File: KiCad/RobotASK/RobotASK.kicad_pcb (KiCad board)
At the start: 2 copper layers, 80 x 50 mm, 13 parts, among them J1 Conn_01x04_Pin, J2 Conn_01x04_Pin, J3 Conn_01x04_Pin, J4 Conn_01x04_Pin, J5 Conn_01x04_Pin, J6 Conn_01x04_Pin, J7 Conn_01x02_Pin, SW2 SW_Omron_B3FS, U1 ATmega328-P, Y1 16MHz

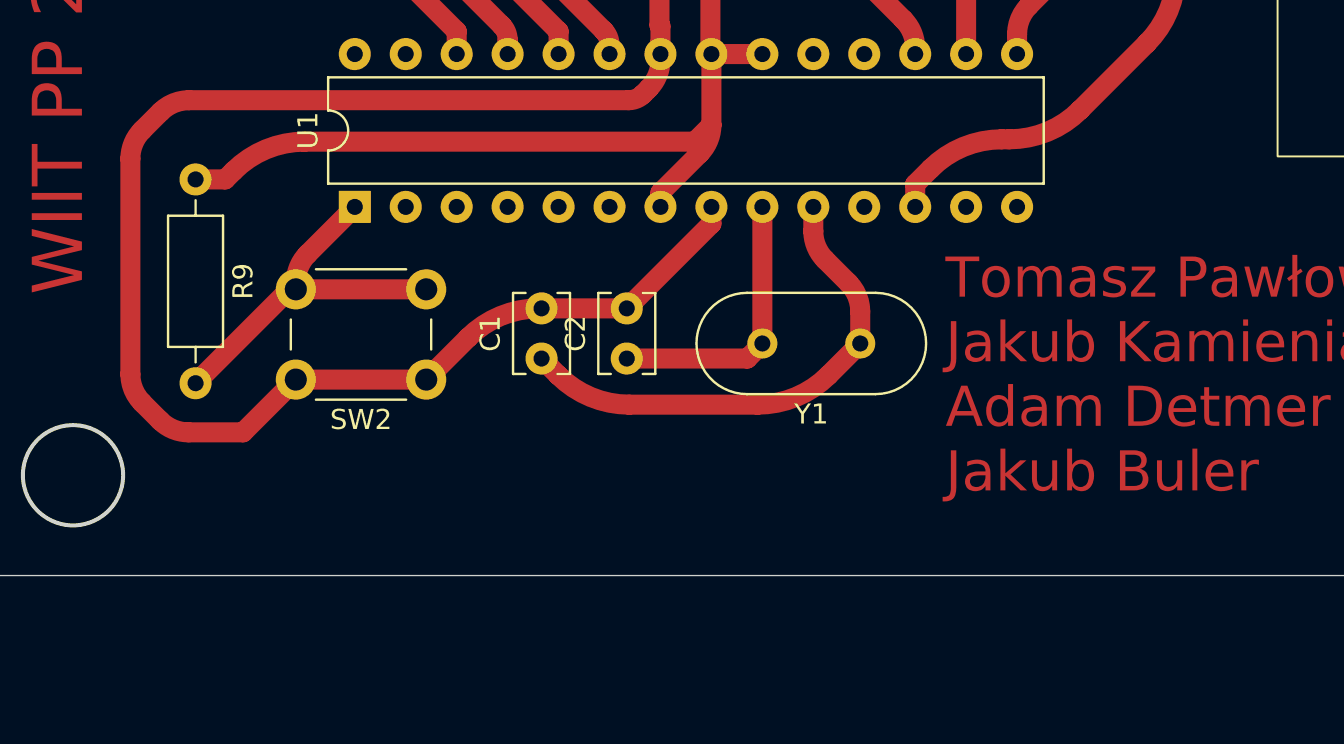
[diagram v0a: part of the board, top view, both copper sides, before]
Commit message: Add pins to quickly reprogram the microprocessor
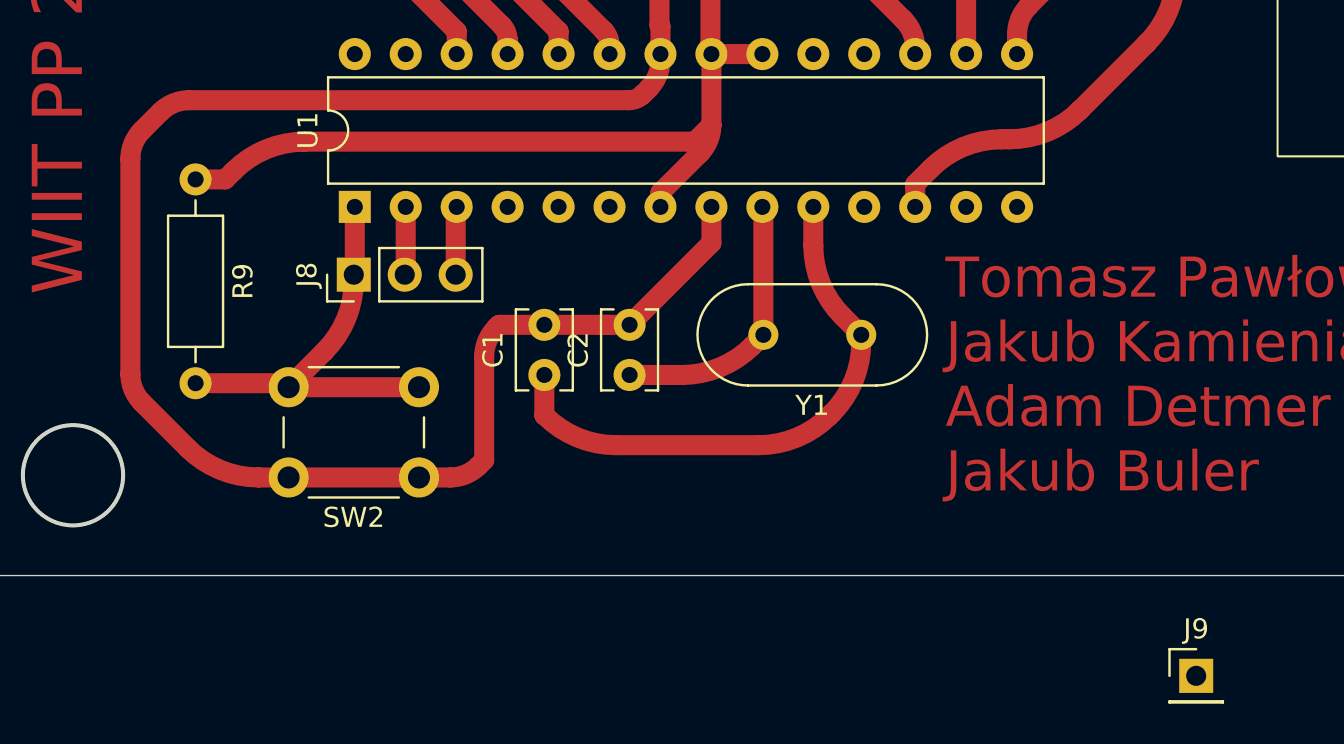
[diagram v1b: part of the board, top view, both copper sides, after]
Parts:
- added J8: Conn_01x03_Pin, Connector_PinHeader_2.54mm:PinHeader_1x03_P2.54mm_Vertical, F.Cu at (89.0, 85.0)
- added J9: Conn_01x01_Pin, Connector_PinHeader_2.54mm:PinHeader_1x01_P2.54mm_Vertical, F.Cu at (131.0, 105.0)
- moved SW2 4.89 mm to (92.2, 95.1)
- moved C1 0.83 mm to (98.5, 90.0)
- moved C2 0.83 mm to (102.8, 90.0)
- moved Y1 0.43 mm to (114.3, 88.0)
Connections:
- U1 pad 2: unconnected-(U1-PD0-Pad2) -> RX
- U1 pad 3: unconnected-(U1-PD1-Pad3) -> TX
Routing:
- net GND: track 156.4 -> 162.7 mm
- net TX: track 0.00 -> 3.40 mm
- net RX: track 0.00 -> 3.40 mm
- net CRY2: track 25.2 -> 28.5 mm
- net ~RESET: track 19.0 -> 21.3 mm

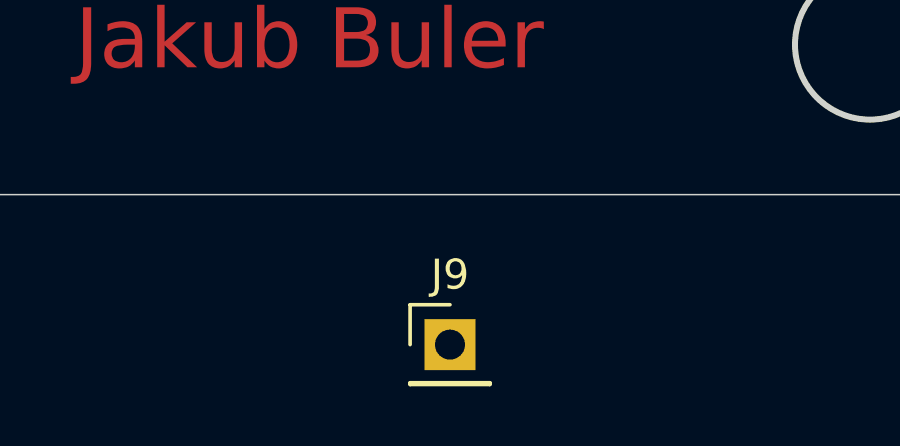
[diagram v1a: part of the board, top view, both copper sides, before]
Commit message: Bez zbędnego pinu GND, update KiCad 8, export ze ścieżkami
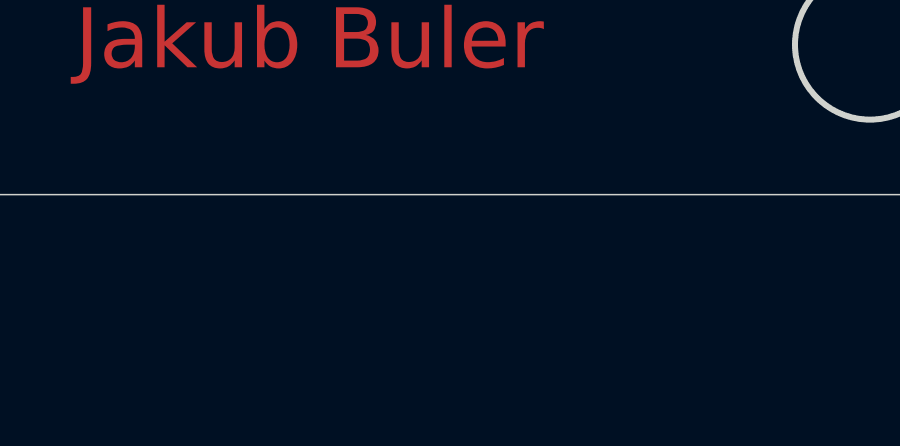
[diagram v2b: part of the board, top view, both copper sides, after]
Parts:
- removed J9: Conn_01x01_Pin, Connector_PinHeader_2.54mm:PinHeader_1x01_P2.54mm_Vertical

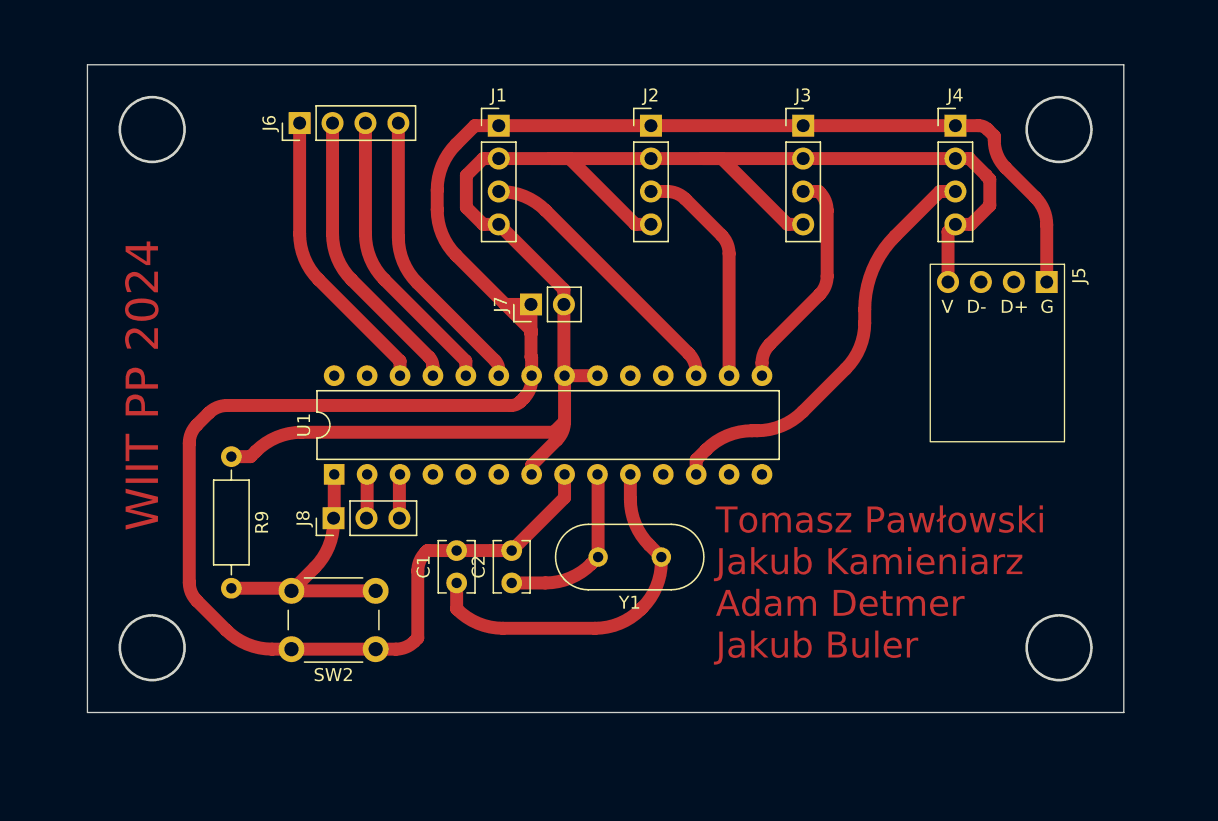
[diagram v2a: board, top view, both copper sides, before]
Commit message: Edit pcb layers
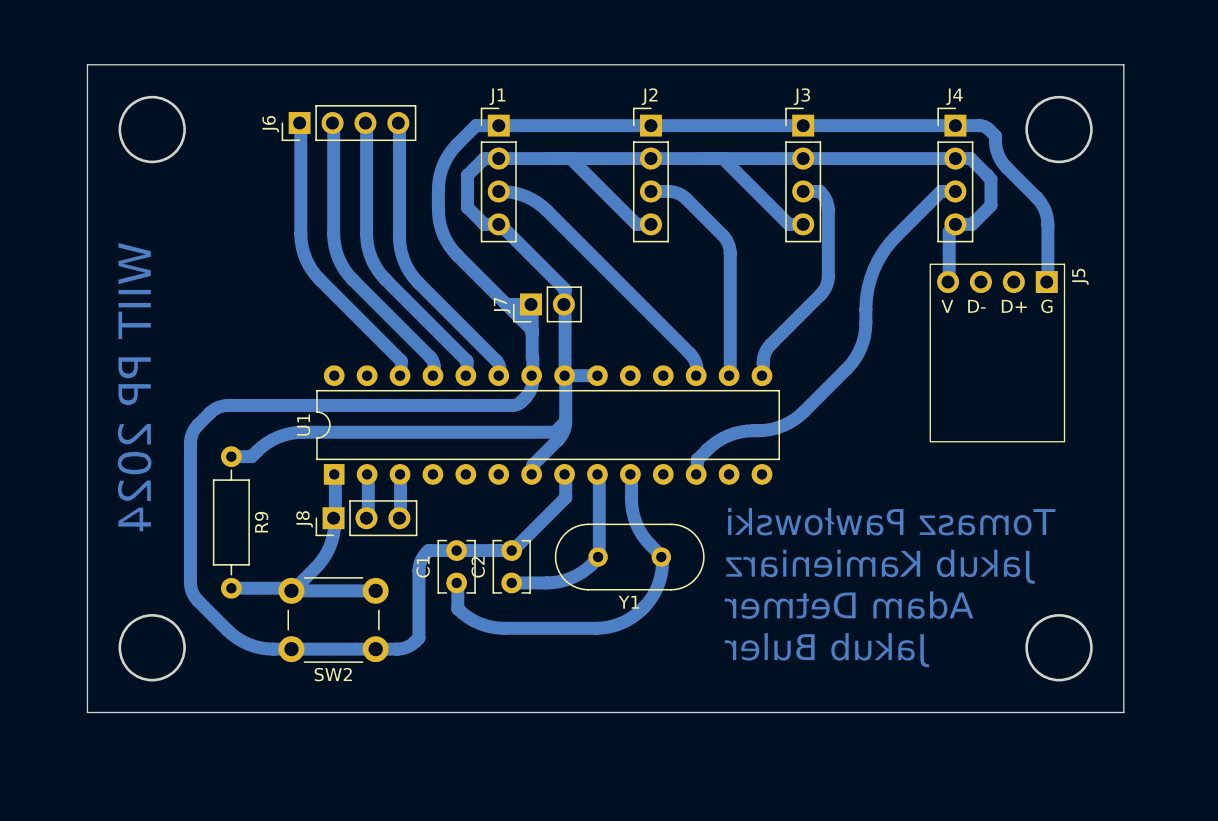
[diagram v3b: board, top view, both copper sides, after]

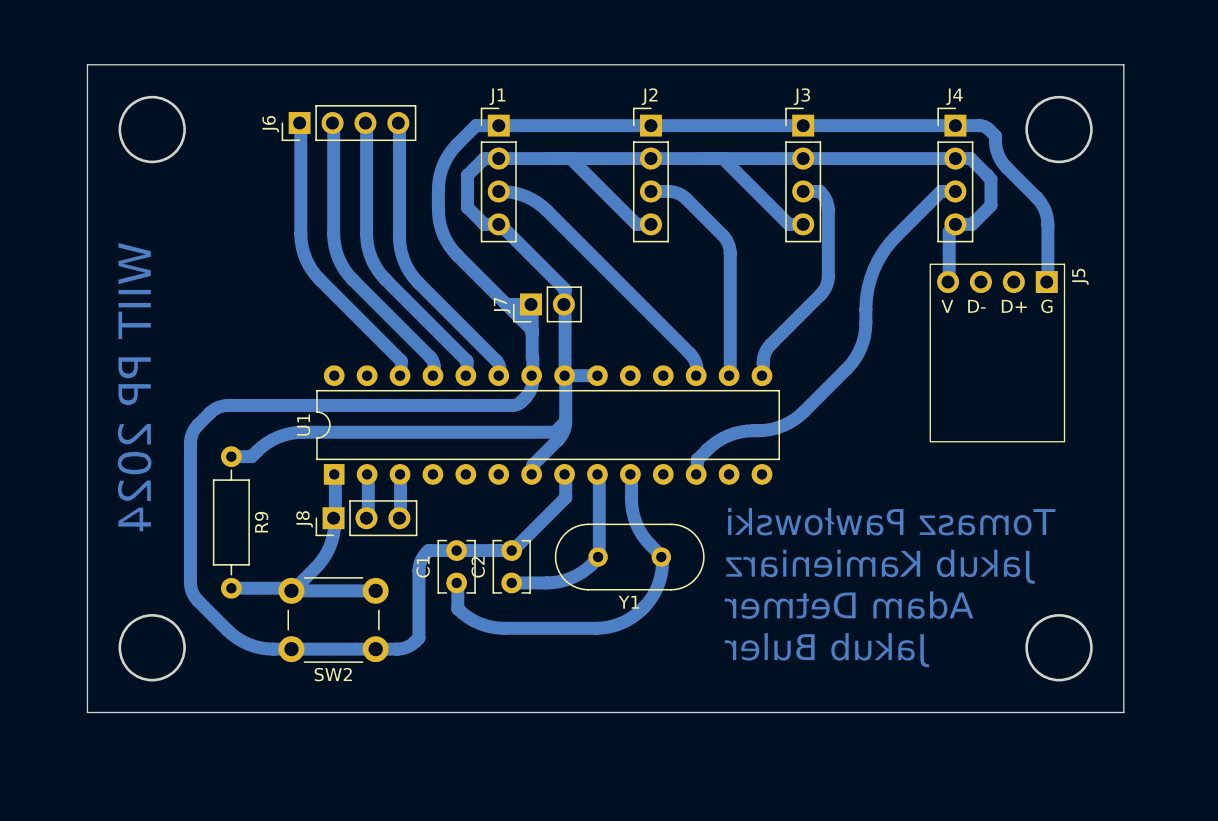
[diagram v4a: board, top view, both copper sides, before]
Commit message: Widen all possible traces, fill edge cuts layer, widen photoresistor PCB by 2mm
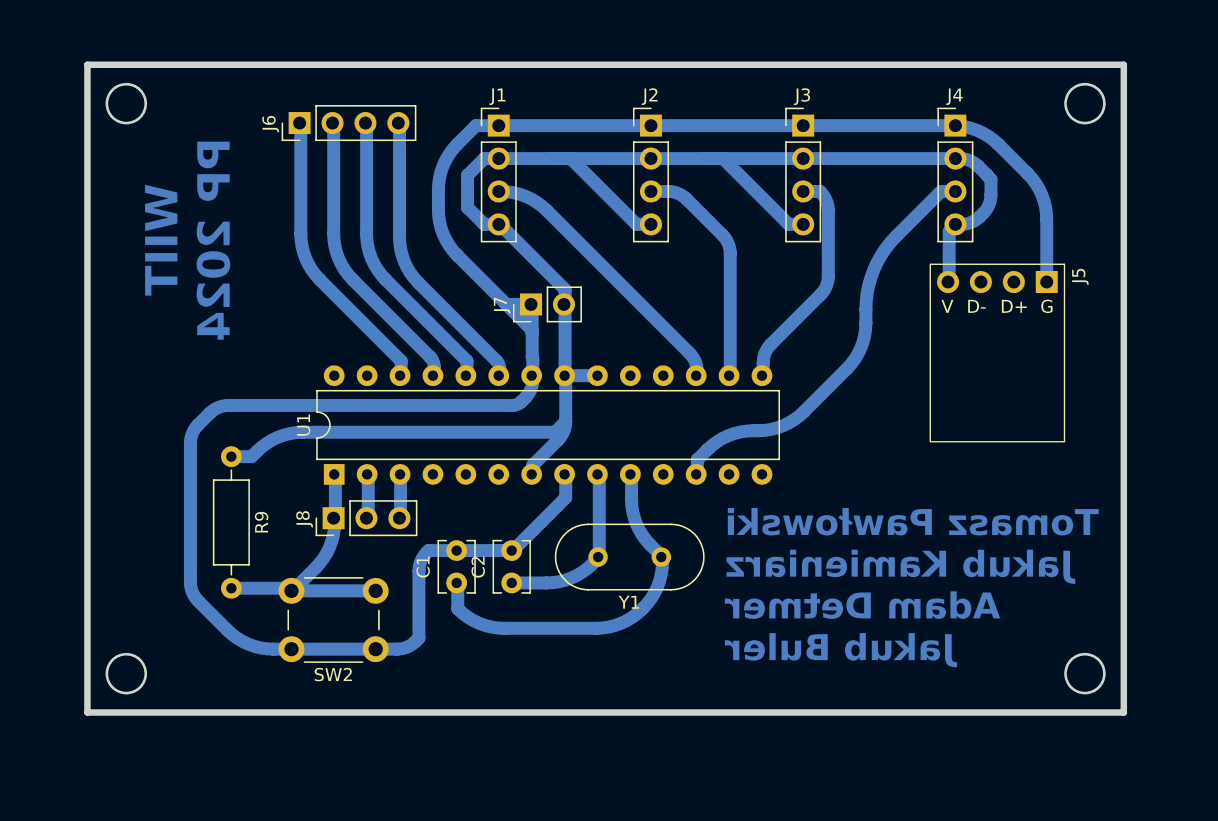
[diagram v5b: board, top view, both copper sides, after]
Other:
- outline, holes or cut-outs redrawn
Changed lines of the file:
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@@
 			(dxfimperialunits yes)
 			(dxfusepcbnewfont yes)
-			(psnegative no)
+			(psnegative yes)
 			(psa4output no)
 			(plotreference yes)
@@
 			(drillshape 1)
 			(scaleselection 1)
-			(outputdirectory "../../wydruki/Termotransfer/")
+			(outputdirectory "../../wydruki/UV/")
 		)
 	)
@@
 	)
 	(gr_circle
-		(center 75 95)
-		(end 77.5 95)
+		(center 73 97)
+		(end 74.5 97)
 		(locked yes)
 		(stroke
@@
 			(type solid)
 		)
-		(fill none)
+		(fill solid)
 		(layer "Edge.Cuts")
 	)
@@
 		(locked yes)
 		(stroke
-			(width 0.05)
+			(width 0.5)
 			(type default)
 		)
@@
 	)
 	(gr_circle
-		(center 145 95)
-		(end 147.5 95)
+		(center 147 97)
+		(end 148.5 97)
 		(locked yes)
 		(stroke
@@
 			(type solid)
 		)
-		(fill none)
+		(fill solid)
 		(layer "Edge.Cuts")
 	)
 	(gr_circle
-		(center 145 55)
-		(end 147.5 55)
+		(center 147 53)
+		(end 148.5 53)
 		(locked yes)
 		(stroke
@@
 			(type solid)
 		)
-		(fill none)
+		(fill solid)
 		(layer "Edge.Cuts")
 	)
 	(gr_circle
-		(center 75 55)
-		(end 77.5 55)
+		(center 73 53)
+		(end 74.5 53)
 		(locked yes)
 		(stroke
@@
 			(type solid)
 		)
-		(fill none)
+		(fill solid)
 		(layer "Edge.Cuts")
 	)
@@
 			(font
 				(size 2 2)
-				(thickness 0.15)
+				(thickness 0.5)
+				(bold yes)
 			)
 			(justify right bottom mirror)
 		)
 	)
-	(gr_text "WIIT PP 2024"
-		(at 75.2 86.2 90)
+	(gr_text "WIIT\nPP 2024"
+		(at 81.28 63.5 90)
 		(layer "B.Cu")
 		(effects
 			(font
 				(size 2.5 2.5)
-				(thickness 0.15)
+				(thickness 0.625)
+				(bold yes)
 			)
-			(justify right bottom mirror)
+			(justify bottom mirror)
 		)
 	)
@@
 	)
 	(segment
+		(start 99.99 54.7)
+		(end 136.804718 54.7)
+		(width 1)
+		(layer "B.Cu")
+		(net 2)
+	)
+	(segment
 		(start 104.33 70.75)
 		(end 104.33 72.561068)
@@
 	)
 	(segment
-		(start 139.582893 54.992893)
-		(end 140.09 55.5)
-		(width 1)
-		(layer "B.Cu")
-		(net 2)
-	)
-	(segment
 		(start 96.175787 87.664213)
 		(end 96.34 87.5)
@@
 	)
 	(segment
-		(start 137.09 54.7)
-		(end 101.84 54.7)
-		(width 1)
-		(layer "B.Cu")
-		(net 2)
-	)
-	(segment
 		(start 104.33 68.5)
 		(end 102.34 68.5)
@@
 	)
 	(segment
-		(start 101.84 54.7)
-		(end 99.99 54.7)
-		(width 1)
-		(layer "B.Cu")
-		(net 2)
-	)
-	(segment
 		(start 101.34 87.5)
 		(end 98.59 87.5)
@@
 	)
 	(segment
-		(start 99.99 54.7)
-		(end 98.554466 56.135534)
-		(width 1)
-		(layer "B.Cu")
-		(net 2)
-	)
-	(segment
 		(start 102.84 87.5)
 		(end 106.92 83.42)
@@
 	)
 	(segment
-		(start 144.14 62.363709)
-		(end 144.14 66.77)
-		(width 1)
-		(layer "B.Cu")
-		(net 2)
-	)
-	(segment
-		(start 140.96868 57.949748)
-		(end 143.261321 60.242389)
-		(width 1)
-		(layer "B.Cu")
-		(net 2)
-	)
-	(segment
-		(start 102.34 68.5)
-		(end 98.554466 64.714466)
-		(width 1)
-		(layer "B.Cu")
-		(net 2)
-	)
-	(segment
 		(start 92.34 95.11)
 		(end 85.84 95.11)
@@
 	)
 	(segment
-		(start 140.09 55.5)
-		(end 140.09 55.828427)
-		(width 1)
-		(layer "B.Cu")
-		(net 2)
-	)
-	(segment
 		(start 95.59 94.25)
 		(end 95.59 89.078427)
@@
 	)
 	(segment
-		(start 137.09 54.7)
-		(end 138.875786 54.7)
+		(start 97.09 61.178932)
+		(end 97.09 59.671068)
 		(width 1)
 		(layer "B.Cu")
@@
 	)
 	(segment
-		(start 104.33 72.561068)
-		(end 104.38 72.611068)
+		(start 98.554466 56.135534)
+		(end 99.99 54.7)
 		(width 1)
 		(layer "B.Cu")
@@
 	)
 	(segment
-		(start 92.34 95.11)
-		(end 93.901573 95.11)
+		(start 144.05 61.945282)
+		(end 144.05 66.77)
 		(width 1)
 		(layer "B.Cu")
@@
 	)
 	(segment
-		(start 97.09 59.671068)
-		(end 97.09 61.178932)
+		(start 102.34 68.5)
+		(end 98.554466 64.714466)
 		(width 1)
 		(layer "B.Cu")
@@
 	)
 	(segment
-		(start 101.84 87.5)
-		(end 101.34 87.5)
+		(start 104.33 72.561068)
+		(end 104.38 72.611068)
 		(width 1)
 		(layer "B.Cu")
 		(net 2)
 	)
-	(arc
-		(start 143.261321 60.242389)
-		(mid 143.911639 61.215659)
-		(end 144.14 62.363709)
+	(segment
+		(start 140.340252 56.164466)
+		(end 142.585534 58.409748)
 		(width 1)
 		(layer "B.Cu")
 		(net 2)
 	)
-	(arc
-		(start 140.96868 57.949748)
-		(mid 140.318361 56.976478)
-		(end 140.09 55.828427)
+	(segment
+		(start 92.34 95.11)
+		(end 93.901573 95.11)
+		(width 1)
+		(layer "B.Cu")
+		(net 2)
+	)
+	(segment
+		(start 101.84 87.5)
+		(end 101.34 87.5)
 		(width 1)
 		(layer "B.Cu")
@@
 	)
 	(arc
-		(start 98.554466 64.714466)
-		(mid 97.470602 63.092349)
-		(end 97.09 61.178932)
+		(start 97.09 59.671068)
+		(mid 97.470602 57.757651)
+		(end 98.554466 56.135534)
 		(width 1)
 		(layer "B.Cu")
@@
 	)
 	(arc
-		(start 78.535786 91.374718)
-		(mid 78.102241 90.725872)
-		(end 77.95 89.960505)
+		(start 140.340252 56.164466)
+		(mid 138.718135 55.080602)
+		(end 136.804718 54.7)
 		(width 1)
 		(layer "B.Cu")
@@
 	)
 	(arc
-		(start 139.582893 54.992893)
-		(mid 139.25847 54.77612)
-		(end 138.875786 54.7)
+		(start 78.535786 91.374718)
+		(mid 78.102241 90.725872)
+		(end 77.95 89.960505)
 		(width 1)
 		(layer "B.Cu")
@@
 	)
 	(arc
-		(start 97.09 59.671068)
-		(mid 97.470602 57.757651)
-		(end 98.554466 56.135534)
+		(start 98.554466 64.714466)
+		(mid 97.470602 63.092349)
+		(end 97.09 61.178932)
 		(width 1)
 		(layer "B.Cu")
@@
 	)
 	(arc
+		(start 142.585534 58.409748)
+		(mid 143.669398 60.031865)
+		(end 144.05 61.945282)
+		(width 1)
+		(layer "B.Cu")
+		(net 2)
+	)
+	(arc
 		(start 96.175787 87.664213)
 		(mid 95.742241 88.31306)
@@
 	(segment
 		(start 137.09 57.24)
-		(end 138.168126 57.24)
+		(end 137.339699 57.24)
 		(width 1)
 		(layer "B.Cu")
@@
 	(segment
 		(start 139.743806 58.846194)
-		(end 139.743806 60.868275)
+		(end 139.743806 60.039848)
 		(width 1)
 		(layer "B.Cu")
@@
 	)
 	(segment
-		(start 138.168126 57.24)
+		(start 138.753913 57.825787)
 		(end 139.46868 58.540554)
 		(width 1)
@@
 	)
 	(segment
-		(start 139.743806 60.868275)
-		(end 138.292081 62.32)
+		(start 139.158019 61.454062)
+		(end 138.877867 61.734214)
 		(width 1)
 		(layer "B.Cu")
@@
 	)
 	(segment
-		(start 138.292081 62.32)
+		(start 137.463654 62.32)
 		(end 137.09 62.32)
 		(width 1)
 		(layer "B.Cu")
+		(net 5)
+	)
+	(arc
+		(start 137.339699 57.24)
+		(mid 138.105066 57.392241)
+		(end 138.753913 57.825787)
+		(width 1)
+		(layer "B.Cu")
+		(net 5)
+	)
+	(arc
+		(start 139.743806 60.039848)
+		(mid 139.591565 60.805215)
+		(end 139.158019 61.454062)
+		(width 1)
+		(layer "B.Cu")
+		(net 5)
+	)
+	(arc
+		(start 138.877867 61.734214)
+		(mid 138.229021 62.167759)
+		(end 137.463654 62.32)
+		(width 1)
+		(layer "B.Cu")
